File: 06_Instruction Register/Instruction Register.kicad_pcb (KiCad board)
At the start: 2 copper layers, 100 x 100 mm, 47 parts, among them J1 Data bus, J2 Instruction Bus, J3 Step-Flag Bus, J4 Input 1, J5 Input 2, U1 74LS377, U2 74LS245, U3 74LS161, U4 74LS157, U5 74LS173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

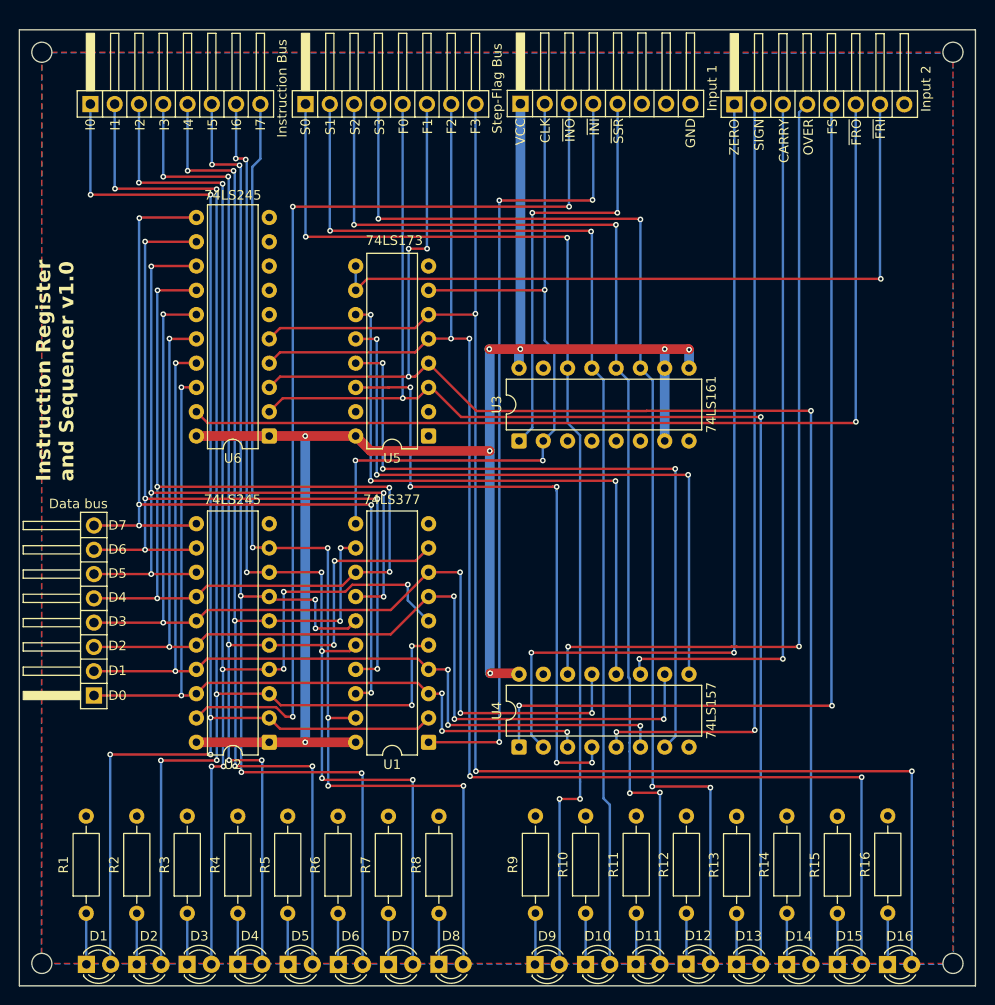
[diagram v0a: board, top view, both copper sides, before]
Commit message: Last revision of the cpu, all boards have been ordered. Implementation to be tested and documented in following commits.
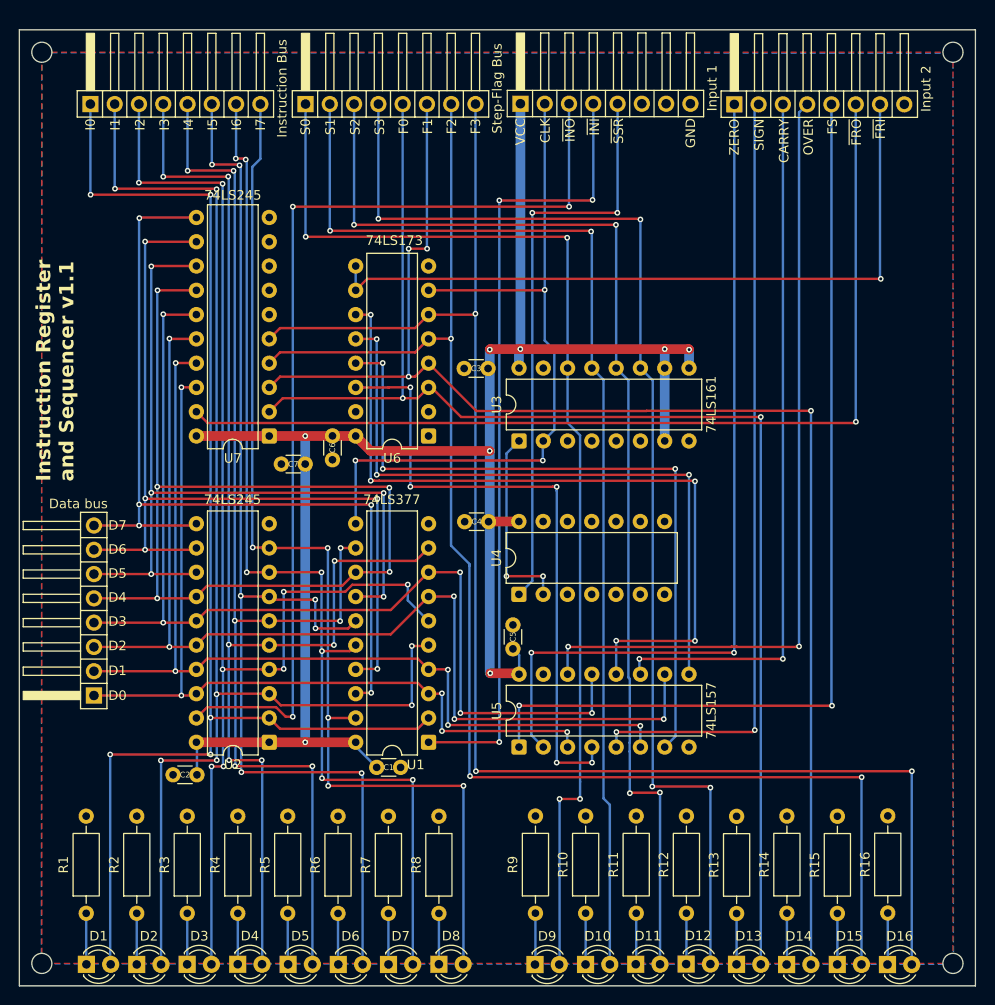
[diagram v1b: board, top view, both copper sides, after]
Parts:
- added C1: 100n, Capacitor_THT:C_Disc_D3.0mm_W1.6mm_P2.50mm, F.Cu at (102.6, 118.5)
- added C2: 100n, Capacitor_THT:C_Disc_D3.0mm_W1.6mm_P2.50mm, F.Cu at (83.8, 119.3)
- added C3: 100n, Capacitor_THT:C_Disc_D3.0mm_W1.6mm_P2.50mm, F.Cu at (114.2, 76.8)
- added C4: 100n, Capacitor_THT:C_Disc_D3.0mm_W1.6mm_P2.50mm, F.Cu at (114.3, 92.8)
- added C5: 100n, Capacitor_THT:C_Disc_D3.0mm_W1.6mm_P2.50mm, F.Cu at (116.8, 106.2)
- added C6: 100n, Capacitor_THT:C_Disc_D3.0mm_W1.6mm_P2.50mm, F.Cu at (98.0, 83.9)
- added C7: 100n, Capacitor_THT:C_Disc_D3.0mm_W1.6mm_P2.50mm, F.Cu at (95.1, 86.8)
- added U4: 74LS04, Package_DIP:DIP-14_W7.62mm, F.Cu at (117.4, 100.5)
- renumbered U4 to U5, U5 to U6, U6 to U7
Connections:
- J4 pad 5: ~{SSR} -> SSR
- U3 pad 1: ~{SSR} -> Net-(U3-~{MR})
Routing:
- net SSR: track 0.00 -> 60.8 mm, vias 0 -> 2
- net ~{SSR}: track 44.8 -> 0.00 mm, vias 2 -> 0
- net Net-(U3-~{MR}): track 0.00 -> 20.4 mm, vias 0 -> 2
- net Net-(U5-Zd): track 64.8 -> 81.3 mm, vias 3 -> 5
- net VCC: track 177.2 -> 190.1 mm
- net F2: track 152.9 -> 151.8 mm, vias 4 -> 3
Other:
- board text added: "Instruction Register and Sequencer v1.1"
- board text removed: "Instruction Register and Sequencer v1.0"

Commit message: Instruction register v1.11 Corrected label ~{SSR} to SSR, no modification to the circuit itself. Active low and high inputs swapped from Input2 to Input1.
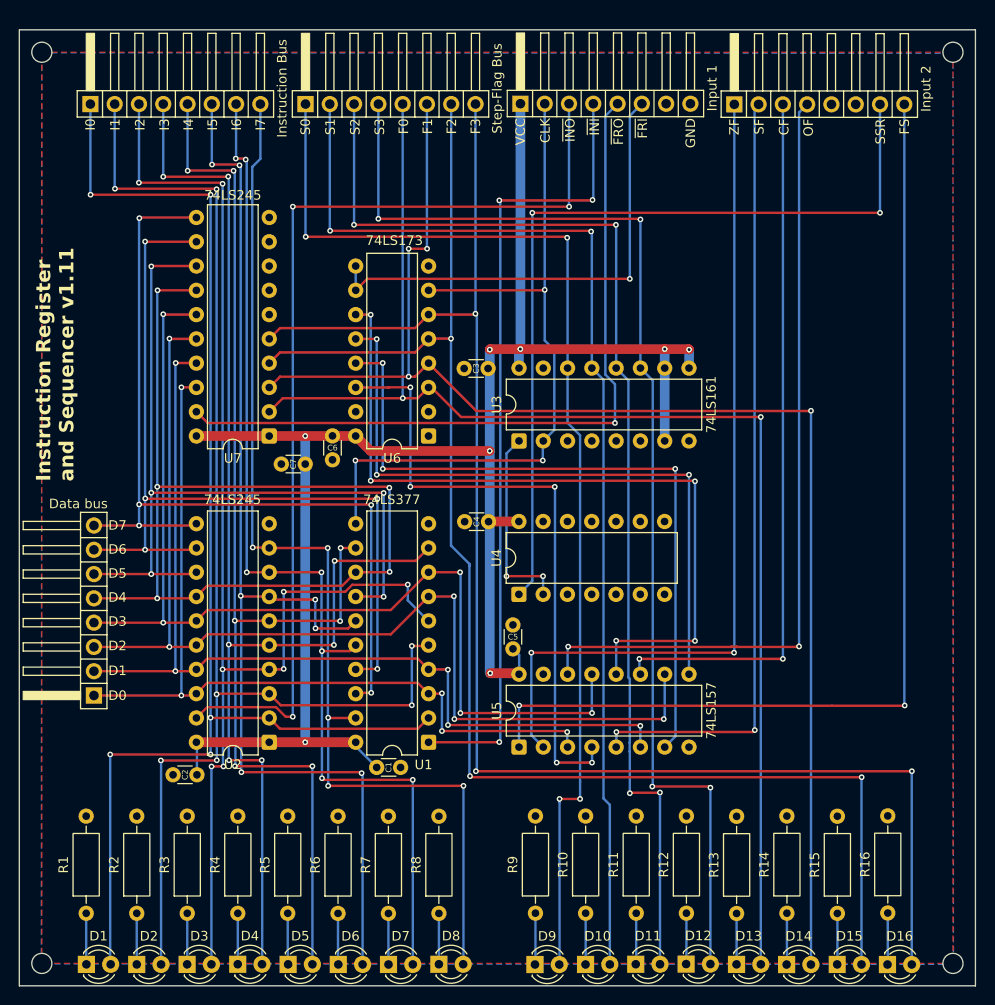
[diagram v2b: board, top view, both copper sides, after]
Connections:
- J4 pad 5: SSR -> ~{FRO}
- J4 pad 6: unconnected-(J4-Pin_6-Pad6) -> ~{FRI}
- J5 pad 5: FS -> unconnected-(J5-Pin_5-Pad5)
- J5 pad 6: ~{FRO} -> unconnected-(J5-Pin_6-Pad6)
- J5 pad 7: ~{FRI} -> SSR
- J5 pad 8: unconnected-(J5-Pin_8-Pad8) -> FS
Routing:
- net SSR: track 60.8 -> 88.2 mm
- net ~{FRI}: track 76.2 -> 50.5 mm
- net ~{FRO}: track 102.7 -> 78.6 mm
- net FS: track 100.0 -> 107.6 mm
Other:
- board text added: "Instruction Register and Sequencer v1.11"
- board text removed: "Instruction Register and Sequencer v1.1"

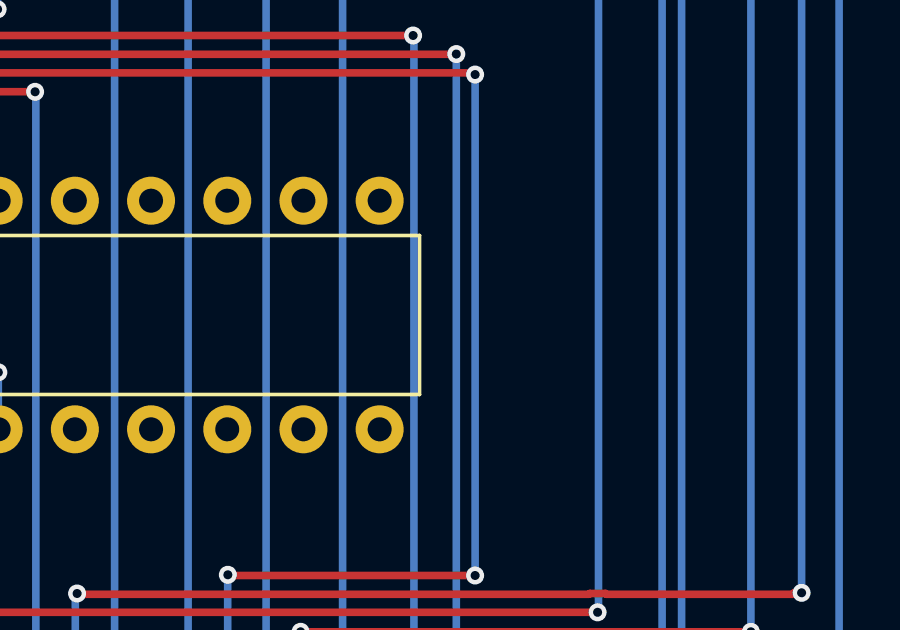
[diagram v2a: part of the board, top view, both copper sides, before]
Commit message: Update 10-01-2026 - Fixed bug on program counter - Fist ISA review, still in draft - Added missing mounting holes on memory modules
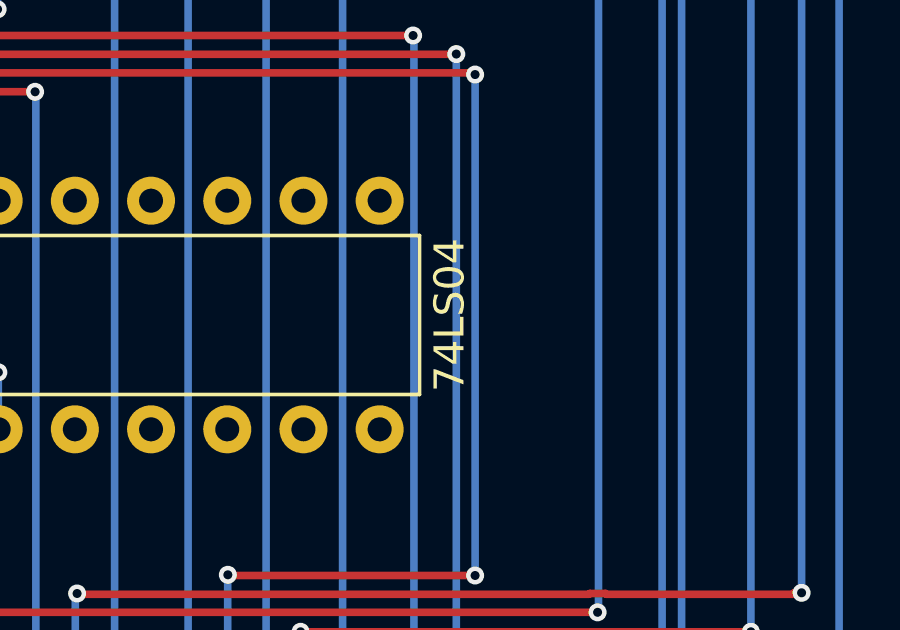
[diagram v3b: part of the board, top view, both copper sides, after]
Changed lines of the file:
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@@
 		(property "Value" "74LS04"
 			(at 3.81 17.57 90)
-			(layer "F.Fab")
+			(layer "F.SilkS")
 			(effects
 				(font
